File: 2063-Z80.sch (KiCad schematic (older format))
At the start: 76 parts, among them J1 Conn_01x05, J10 Conn_01x07, J2 DM3D-SF(41), J3 Conn_02x20_Counter_Clockwise, J4 Conn_02x05_Odd_Even, J5 Conn_02x05_Odd_Even, J6 0548190519, J7 Conn_02x13_Top_Bottom, J8 Conn_01x05, J9 Conn_01x02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

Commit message: BOM updates.
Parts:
- R1, R3, R5: Description (none) -> ‎CF18JT2K70‎; Digi-Key_PN (none) -> CF18JT2K70CT-ND
- R11, R12: Description (none) -> ‎CF18JT1K00‎; Digi-Key_PN (none) -> CF18JT1K00CT-ND‎
- R2, R4, R6: Description (none) -> ‎CF18JT4K70‎; Digi-Key_PN (none) -> CF18JT2K70CT-ND
- R8, R9: Description (none) -> ‎CF18JT680R‎; Digi-Key_PN (none) -> CF18JT680RCT-ND‎
- RN1, RN2, RN3, RN4, RN5: Description (none) -> ‎4609X-101-103LF‎
- U2: Description (none) -> ‎AS6C4008-55PIN‎; Digi-Key_PN (none) -> 1450-1178-5-ND‎
- U3: Description (none) -> ‎SST39SF010A-70-4C-PHE; Digi-Key_PN (none) -> SST39SF010A-70-4C-PHE-ND‎

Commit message: Add jumpers for getting the SIO baud rate clock direct from X2 (EZ-bypass the CTC) Missing white-slug on J10 Show R8 & R9 as 680 ohms on silkscreen Change part number of the NAND gate to 74HCT132E (Schmitt) Move reset button to the right (so can read silk labels on J10)
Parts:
- added J11: Conn_02x03_Odd_Even, Connector_PinHeader_2.54mm:PinHeader_2x03_P2.54mm_Vertical, symbol Connector_Generic:Conn_02x03_Odd_Even
- Q1: footprint Package_TO_SOT_THT:TO-92L_Inline -> Package_TO_SOT_THT:TO-92L
- U11: value 74LS00 -> 74HCT132E
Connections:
- net BAUD_CLK: now also J11.1 (Pin_1), J11.2 (Pin_2)
- net SIO_CLKA: now also J11.4 (Pin_4); no longer U4.8 (ZC/TO1)
- net SIO_CLKB: now also J11.3 (Pin_3); no longer U4.9 (ZC/TO2)
- new net CTC_CLKA: J11.6 (Pin_6), U4.8 (ZC/TO1)
- new net CTC_CLKB: J11.5 (Pin_5), U4.9 (ZC/TO2)
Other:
- note added: "BAUD Rate CLK Select"
- moved on the sheet: D1, D2, R8, R9, X1, X2

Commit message: Add another 74LS32 for 512K memory support. Move 3.3v reg on back under the SD card. Use surface-mount caps for 3.3v power. Add alternate SMT footprints for X1 and X2.
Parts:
- removed J9: Conn_01x02, Connector_PinHeader_2.54mm:PinHeader_1x02_P2.54mm_Vertical, symbol Connector_Generic:Conn_01x02
- removed R13: 10K, Resistor_THT:R_Axial_DIN0204_L3.6mm_D1.6mm_P5.08mm_Horizontal, symbol Device:R
- added U13: 74LS32, Package_DIP:DIP-14_W7.62mm_Socket, symbol 74xx:74LS32
- added Y1: XX, Oscillator:Oscillator_SMD_IQD_IQXO70-4Pin_7.5x5.0mm_HandSoldering, symbol dk_Oscillators:XLH536025_000000I
- added Y2: CSX-750FBC3686400T, Oscillator:Oscillator_SMD_IQD_IQXO70-4Pin_7.5x5.0mm_HandSoldering, symbol dk_Oscillators:XLH536025_000000I
- C17: footprint Capacitor_THT:C_Disc_D3.0mm_W2.0mm_P2.50mm -> Capacitor_SMD:C_0805_2012Metric_Pad1.18x1.45mm_HandSolder
- C18: footprint Capacitor_THT:CP_Radial_D5.0mm_P2.50mm -> Capacitor_SMD:C_0805_2012Metric_Pad1.18x1.45mm_HandSolder
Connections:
- net +5V: now also U13.14 (VCC), Y1.4 (VDD), Y2.4 (VDD)
- net A15: now also U13.1, U13.12, U13.4, U13.9; no longer U10.12, U10.9, U2.31 (A15)
- net BAUD_CLK: now also Y2.3 (OUT)
- net CLK: now also Y1.3 (OUT)
- net DISC_LED: now also U11.8; no longer U6.9 (O3)
- net GND: now also U10.12, U11.9, U13.7 (GND), Y1.2 (GND), Y2.2 (GND); no longer U2.1 (A18)
- net LO_BANK_A16: now also U6.15 (O5), U13.5; no longer U10.13, U6.16 (O6)
- net LO_BANK_A17: now also U6.16 (O6), U13.10; no longer U10.10, U6.19 (O7)
- net SD5_MOSI: now also U11.10
- net ~DTRA: now also U10.10, U10.9; no longer U11.10, U11.9
- net ~PRN_INIT: now also U10.8; no longer U11.8
- net ~PRN_LF: now also U10.11; no longer U6.15 (O5)
- net ~PRN_STROBE: now also U6.9 (O3); no longer U6.12 (O4)
- net ~RTSA: now reaches U5.17 (~RTSA)
- net ~RTSA: now also U10.13
- net A16 renamed BA16
- net BA16: now also U13.6; no longer U10.11
- net A17 renamed BA17
- net BA17: now also U13.8
- new net BA15: U13.3, U2.31 (A15)
- new net BA18: U13.11, U2.1 (A18)
- new net LO_BANK_A15: U13.2, U6.12 (O4)
- new net LO_BANK_A18: U13.13, U6.19 (O7)
- no-connect marks 33 -> 34
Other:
- note added: "3.6864MHZ"
- note added: "System Clock"
- note added: "Y1 is an alternate\n footprint for X1"
- note added: "Y2 is an alternate\n footprint for X2"
- note removed: "Remove J9 for 128K SRAM9"
- moved on the sheet: C10, C13, C14, C15, C16, C18, C19, C20, C21, C22, C23, C3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

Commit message: Fix inverted DISC_LED signal. Create composite oscillator footprints for X1 and X2. Tidy up the sensitive clock-tracks.
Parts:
- removed Y1: XX, Oscillator:Oscillator_SMD_IQD_IQXO70-4Pin_7.5x5.0mm_HandSoldering, symbol dk_Oscillators:XLH536025_000000I
- removed Y2: CSX-750FBC3686400T, Oscillator:Oscillator_SMD_IQD_IQXO70-4Pin_7.5x5.0mm_HandSoldering, symbol dk_Oscillators:XLH536025_000000I
- added C24: .1, Capacitor_SMD:C_0805_2012Metric_Pad1.15x1.40mm_HandSolder, symbol Device:C_Small
- X1: value ‎ECS-2100AX-049‎ -> ACH-10.000MHZ-EK; footprint Oscillator:Oscillator_DIP-8 -> jb-footprint:Oscillator_DIP-8_combo; Digi-Key_PN XC1159-ND‎ -> 535-9167-5-ND; MPN ECS-2100AX-049‎ -> ACH-10.000MHZ-EK
- X2: value ‎ECS-2100AX-049‎ -> ECS-2100A-018; footprint Oscillator:Oscillator_DIP-8 -> jb-footprint:Oscillator_DIP-8_combo; Digi-Key_PN XC1159-ND‎ -> XC231-ND‎; MPN ECS-2100AX-049‎ -> ‎ECS-2100A-018‎
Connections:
- net +5V: now also C24.1; no longer R8.2
- net DISC_LED: now also D2.2 (A); no longer D2.1 (K)
- net GND: now also R8.2, U10.10, C24.2; no longer U11.9
- net SD5_MOSI: no longer U11.10
- net ~DTRA: no longer U10.10
- net at R8.1: now also D2.1 (K); no longer D2.2 (A)
- net SD5_SSEL renamed ~SD5_SSEL
- net ~SD5_SSEL: now also U11.10, U11.9
- net SD_SSEL renamed ~SD_SSEL
- no-connect marks 34 -> 32
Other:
- note added: "1.8432MHZ"
- note added: "Shadow FLASH Select Logic"
- note removed: "3.6864MHZ"
- note removed: "4.9152MHZ"
- note removed: "FLASH Startup Select Logic"
- note removed: "Y1 is an alternate\n footprint for X1"
- note removed: "Y2 is an alternate\n footprint for X2"
- moved on the sheet: C20, C23, D2, D3, J11, J6, Q1, R11, R12, RN1, RN2, RN4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

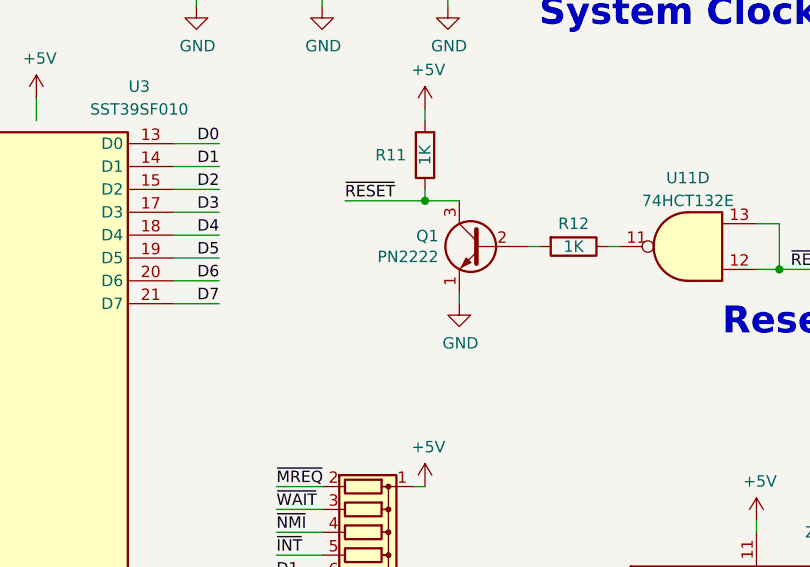
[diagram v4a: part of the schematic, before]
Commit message: Change .1uF parts on BOM.
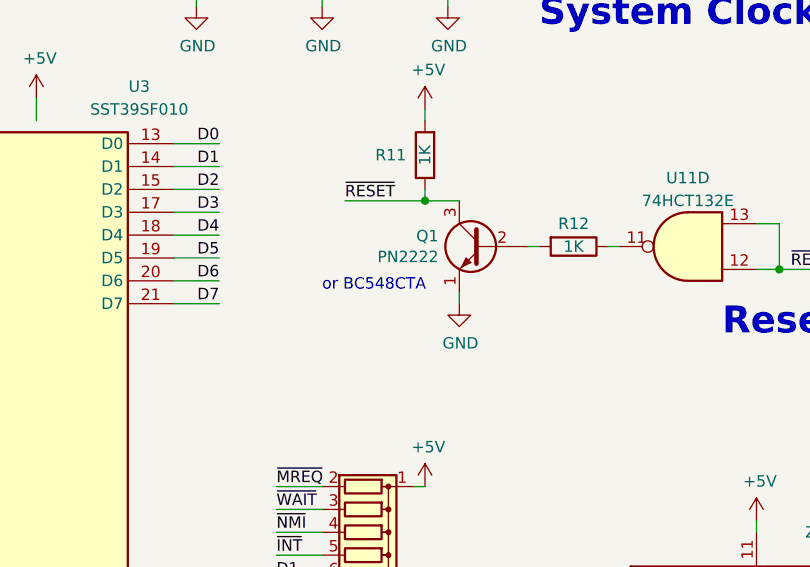
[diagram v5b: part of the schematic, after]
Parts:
- C1, C10, C11, C12, C13, C14, C15, C16, C2, C20, C21, C22, C23, C3, C4, C5, C6, C7, C8, C9: Digi-Key_PN 399-9976-ND -> 399-9859-1-ND‎; MPN (none) -> ‎C315C104M5U5TA7303‎
- C17: Digi-Key_PN 399-9976-ND -> (none)
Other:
- note added: "or ‎BC548CTA‎"
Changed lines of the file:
@@
 F 2 "Capacitor_THT:C_Disc_D3.0mm_W2.0mm_P2.50mm" H 4000 950 50  0001 C CNN
 F 3 "~" H 4000 950 50  0001 C CNN
-F 4 "399-9976-ND" H 4000 950 50  0001 C CNN "Digi-Key_PN"
+F 4 "399-9859-1-ND‎" H 4000 950 50  0001 C CNN "Digi-Key_PN"
+F 5 "‎C315C104M5U5TA7303‎" H 4000 950 50  0001 C CNN "MPN"
 	1    4000 950
 	1    0    0    -1
@@
 F 2 "Capacitor_THT:C_Disc_D3.0mm_W2.0mm_P2.50mm" H 4300 950 50  0001 C CNN
 F 3 "~" H 4300 950 50  0001 C CNN
-F 4 "399-9976-ND" H 4300 950 50  0001 C CNN "Digi-Key_PN"
+F 4 "399-9859-1-ND‎" H 4300 950 50  0001 C CNN "Digi-Key_PN"
+F 5 "‎C315C104M5U5TA7303‎" H 4300 950 50  0001 C CNN "MPN"
 	1    4300 950
 	1    0    0    -1
@@
 F 2 "Capacitor_THT:C_Disc_D3.0mm_W2.0mm_P2.50mm" H 4600 950 50  0001 C CNN
 F 3 "~" H 4600 950 50  0001 C CNN
-F 4 "399-9976-ND" H 4600 950 50  0001 C CNN "Digi-Key_PN"
+F 4 "399-9859-1-ND‎" H 4600 950 50  0001 C CNN "Digi-Key_PN"
+F 5 "‎C315C104M5U5TA7303‎" H 4600 950 50  0001 C CNN "MPN"
 	1    4600 950
 	1    0    0    -1
@@
 F 2 "Capacitor_THT:C_Disc_D3.0mm_W2.0mm_P2.50mm" H 4900 950 50  0001 C CNN
 F 3 "~" H 4900 950 50  0001 C CNN
-F 4 "399-9976-ND" H 4900 950 50  0001 C CNN "Digi-Key_PN"
+F 4 "399-9859-1-ND‎" H 4900 950 50  0001 C CNN "Digi-Key_PN"
+F 5 "‎C315C104M5U5TA7303‎" H 4900 950 50  0001 C CNN "MPN"
 	1    4900 950
 	1    0    0    -1
@@
 F 2 "Capacitor_THT:C_Disc_D3.0mm_W2.0mm_P2.50mm" H 5200 950 50  0001 C CNN
 F 3 "~" H 5200 950 50  0001 C CNN
-F 4 "399-9976-ND" H 5200 950 50  0001 C CNN "Digi-Key_PN"
+F 4 "399-9859-1-ND‎" H 5200 950 50  0001 C CNN "Digi-Key_PN"
+F 5 "‎C315C104M5U5TA7303‎" H 5200 950 50  0001 C CNN "MPN"
 	1    5200 950
 	1    0    0    -1
@@
 F 2 "Capacitor_THT:C_Disc_D3.0mm_W2.0mm_P2.50mm" H 7000 8400 50  0001 C CNN
 F 3 "~" H 7000 8400 50  0001 C CNN
-F 4 "399-9976-ND" H 7000 8400 50  0001 C CNN "Digi-Key_PN"
+F 4 "399-9859-1-ND‎" H 7000 8400 50  0001 C CNN "Digi-Key_PN"
+F 5 "‎C315C104M5U5TA7303‎" H 7000 8400 50  0001 C CNN "MPN"
 	1    7000 8400
 	1    0    0    -1
@@
 F 2 "Capacitor_THT:C_Disc_D3.0mm_W2.0mm_P2.50mm" H 9150 8350 50  0001 C CNN
 F 3 "~" H 9150 8350 50  0001 C CNN
-F 4 "399-9976-ND" H 9150 8350 50  0001 C CNN "Digi-Key_PN"
+F 4 "399-9859-1-ND‎" H 9150 8350 50  0001 C CNN "Digi-Key_PN"
+F 5 "‎C315C104M5U5TA7303‎" H 9150 8350 50  0001 C CNN "MPN"
 	1    9150 8350
 	1    0    0    -1
@@
 F 2 "Capacitor_THT:C_Disc_D3.0mm_W2.0mm_P2.50mm" H 9200 8750 50  0001 C CNN
 F 3 "~" H 9200 8750 50  0001 C CNN
-F 4 "399-9976-ND" H 9200 8750 50  0001 C CNN "Digi-Key_PN"
+F 4 "399-9859-1-ND‎" H 9200 8750 50  0001 C CNN "Digi-Key_PN"
+F 5 "‎C315C104M5U5TA7303‎" H 9200 8750 50  0001 C CNN "MPN"
 	1    9200 8750
 	0    1    1    0
@@
 F 2 "Capacitor_THT:C_Disc_D3.0mm_W2.0mm_P2.50mm" H 9200 9050 50  0001 C CNN
 F 3 "~" H 9200 9050 50  0001 C CNN
-F 4 "399-9976-ND" H 9200 9050 50  0001 C CNN "Digi-Key_PN"
+F 4 "399-9859-1-ND‎" H 9200 9050 50  0001 C CNN "Digi-Key_PN"
+F 5 "‎C315C104M5U5TA7303‎" H 9200 9050 50  0001 C CNN "MPN"
 	1    9200 9050
 	0    1    1    0
@@
 F 2 "Capacitor_THT:C_Disc_D3.0mm_W2.0mm_P2.50mm" H 5500 950 50  0001 C CNN
 F 3 "~" H 5500 950 50  0001 C CNN
-F 4 "399-9976-ND" H 5500 950 50  0001 C CNN "Digi-Key_PN"
+F 4 "399-9859-1-ND‎" H 5500 950 50  0001 C CNN "Digi-Key_PN"
+F 5 "‎C315C104M5U5TA7303‎" H 5500 950 50  0001 C CNN "MPN"
 	1    5500 950
 	-1   0    0    1
@@
 F 2 "Capacitor_THT:C_Disc_D3.0mm_W2.0mm_P2.50mm" H 5200 1550 50  0001 C CNN
 F 3 "~" H 5200 1550 50  0001 C CNN
-F 4 "399-9976-ND" H 5200 1550 50  0001 C CNN "Digi-Key_PN"
+F 4 "399-9859-1-ND‎" H 5200 1550 50  0001 C CNN "Digi-Key_PN"
+F 5 "‎C315C104M5U5TA7303‎" H 5200 1550 50  0001 C CNN "MPN"
 	1    5200 1550
 	1    0    0    -1
@@
 F 2 "Capacitor_THT:C_Disc_D3.0mm_W2.0mm_P2.50mm" H 5500 1550 50  0001 C CNN
 F 3 "~" H 5500 1550 50  0001 C CNN
-F 4 "399-9976-ND" H 5500 1550 50  0001 C CNN "Digi-Key_PN"
+F 4 "399-9859-1-ND‎" H 5500 1550 50  0001 C CNN "Digi-Key_PN"
+F 5 "‎C315C104M5U5TA7303‎" H 5500 1550 50  0001 C CNN "MPN"
 	1    5500 1550
 	1    0    0    -1
@@
 F 2 "Capacitor_THT:C_Disc_D3.0mm_W2.0mm_P2.50mm" H 3700 1550 50  0001 C CNN
 F 3 "~" H 3700 1550 50  0001 C CNN
-F 4 "399-9976-ND" H 3700 1550 50  0001 C CNN "Digi-Key_PN"
+F 4 "399-9859-1-ND‎" H 3700 1550 50  0001 C CNN "Digi-Key_PN"
+F 5 "‎C315C104M5U5TA7303‎" H 3700 1550 50  0001 C CNN "MPN"
 	1    3700 1550
 	1    0    0    -1
@@
 F 2 "Capacitor_THT:C_Disc_D3.0mm_W2.0mm_P2.50mm" H 4000 1550 50  0001 C CNN
 F 3 "~" H 4000 1550 50  0001 C CNN
-F 4 "399-9976-ND" H 4000 1550 50  0001 C CNN "Digi-Key_PN"
+F 4 "399-9859-1-ND‎" H 4000 1550 50  0001 C CNN "Digi-Key_PN"
+F 5 "‎C315C104M5U5TA7303‎" H 4000 1550 50  0001 C CNN "MPN"
 	1    4000 1550
 	1    0    0    -1
@@
 F 2 "Capacitor_THT:C_Disc_D3.0mm_W2.0mm_P2.50mm" H 4300 1550 50  0001 C CNN
 F 3 "~" H 4300 1550 50  0001 C CNN
-F 4 "399-9976-ND" H 4300 1550 50  0001 C CNN "Digi-Key_PN"
+F 4 "399-9859-1-ND‎" H 4300 1550 50  0001 C CNN "Digi-Key_PN"
+F 5 "‎C315C104M5U5TA7303‎" H 4300 1550 50  0001 C CNN "MPN"
 	1    4300 1550
 	1    0    0    -1
@@
 F 2 "Capacitor_THT:C_Disc_D3.0mm_W2.0mm_P2.50mm" H 4600 1550 50  0001 C CNN
 F 3 "~" H 4600 1550 50  0001 C CNN
-F 4 "399-9976-ND" H 4600 1550 50  0001 C CNN "Digi-Key_PN"
+F 4 "399-9859-1-ND‎" H 4600 1550 50  0001 C CNN "Digi-Key_PN"
+F 5 "‎C315C104M5U5TA7303‎" H 4600 1550 50  0001 C CNN "MPN"
 	1    4600 1550
 	1    0    0    -1
@@
 F 2 "Capacitor_SMD:C_0805_2012Metric_Pad1.18x1.45mm_HandSolder" H 13450 8200 50  0001 C CNN
 F 3 "~" H 13450 8200 50  0001 C CNN
-F 4 "399-9976-ND" H 13450 8200 50  0001 C CNN "Digi-Key_PN"
+F 4 "" H 13450 8200 50  0001 C CNN "Digi-Key_PN"
 	1    13450 8200
 	1    0    0    -1
@@
 F 2 "Capacitor_THT:C_Disc_D3.0mm_W2.0mm_P2.50mm" H 4900 1550 50  0001 C CNN
 F 3 "~" H 4900 1550 50  0001 C CNN
-F 4 "399-9976-ND" H 4900 1550 50  0001 C CNN "Digi-Key_PN"
+F 4 "399-9859-1-ND‎" H 4900 1550 50  0001 C CNN "Digi-Key_PN"
+F 5 "‎C315C104M5U5TA7303‎" H 4900 1550 50  0001 C CNN "MPN"
 	1    4900 1550
 	1    0    0    -1
@@
 F 2 "Capacitor_THT:C_Disc_D3.0mm_W2.0mm_P2.50mm" H 10100 3050 50  0001 C CNN
 F 3 "~" H 10100 3050 50  0001 C CNN
-F 4 "399-9976-ND" H 10100 3050 50  0001 C CNN "Digi-Key_PN"
+F 4 "399-9859-1-ND‎" H 10100 3050 50  0001 C CNN "Digi-Key_PN"
+F 5 "‎C315C104M5U5TA7303‎" H 10100 3050 50  0001 C CNN "MPN"
 	1    10100 3050
 	1    0    0    -1
@@
 F 2 "Capacitor_THT:C_Disc_D3.0mm_W2.0mm_P2.50mm" H 3700 950 50  0001 C CNN
 F 3 "~" H 3700 950 50  0001 C CNN
-F 4 "399-9976-ND" H 3700 950 50  0001 C CNN "Digi-Key_PN"
+F 4 "399-9859-1-ND‎" H 3700 950 50  0001 C CNN "Digi-Key_PN"
+F 5 "‎C315C104M5U5TA7303‎" H 3700 950 50  0001 C CNN "MPN"
 	1    3700 950
 	1    0    0    -1
@@
 F 2 "Capacitor_THT:C_Disc_D3.0mm_W2.0mm_P2.50mm" H 5850 950 50  0001 C CNN
 F 3 "~" H 5850 950 50  0001 C CNN
-F 4 "399-9976-ND" H 5850 950 50  0001 C CNN "Digi-Key_PN"
+F 4 "399-9859-1-ND‎" H 5850 950 50  0001 C CNN "Digi-Key_PN"
+F 5 "‎C315C104M5U5TA7303‎" H 5850 950 50  0001 C CNN "MPN"
 	1    5850 950
 	1    0    0    -1
@@
 	1    0    0    -1
 $EndComp
+Text Notes 7250 3050 0    50   ~ 0
+or ‎BC548CTA‎
 $EndSCHEMATC

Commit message: Add pull up to SIO (and CTC) IEI.
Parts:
- added R10, R13: 10K, Resistor_THT:R_Axial_DIN0204_L3.6mm_D1.6mm_P5.08mm_Horizontal, symbol Device:R
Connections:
- net +5V: now also R10.2, R13.2; no longer U4.13 (IEI)
- net CTC_IEO: now also R10.1
- new net: R13.1, U4.13 (IEI)
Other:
- note added: "Populate R10 when the CTC is not present. \nElse optional."
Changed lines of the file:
@@
 	11550 6350 11900 6350
-Wire Wire Line
-	11550 6250 11900 6250
 Wire Wire Line
 	11550 6150 11900 6150
@@
 Text Label 7700 6400 2    50   ~ 0
 A0
-$Comp
-L power:+5V #PWR0143
-U 1 1 62D73A3F
-P 5900 7050
-F 0 "#PWR0143" H 5900 6900 50  0001 C CNN
-F 1 "+5V" H 5915 7223 50  0000 C CNN
-F 2 "" H 5900 7050 50  0001 C CNN
-F 3 "" H 5900 7050 50  0001 C CNN
-	1    5900 7050
-	1    0    0    -1
-$EndComp
-Wire Wire Line
-	6350 7050 5900 7050
 Text Label 6000 7150 0    50   ~ 0
 CTC_IEO
@@
 Text Notes 7250 3050 0    50   ~ 0
 or ‎BC548CTA‎
+$Comp
+L Device:R R10
+U 1 1 614B473D
+P 11350 6100
+F 0 "R10" V 11450 6100 50  0000 C CNN
+F 1 "10K" V 11350 6100 50  0000 C CNN
+F 2 "Resistor_THT:R_Axial_DIN0204_L3.6mm_D1.6mm_P5.08mm_Horizontal" V 11280 6100 50  0001 C CNN
+F 3 "~" H 11350 6100 50  0001 C CNN
+	1    11350 6100
+	-1   0    0    1
+$EndComp
+Wire Wire Line
+	11350 6250 11900 6250
+Wire Wire Line
+	11350 5950 11350 5900
+$Comp
+L power:+5V #PWR014
+U 1 1 615C4A3C
+P 11350 5900
+F 0 "#PWR014" H 11350 5750 50  0001 C CNN
+F 1 "+5V" H 11365 6073 50  0000 C CNN
+F 2 "" H 11350 5900 50  0001 C CNN
+F 3 "" H 11350 5900 50  0001 C CNN
+	1    11350 5900
+	1    0    0    -1
+$EndComp
+$Comp
+L Device:R R13
+U 1 1 615CB44E
+P 5800 6900
+F 0 "R13" V 5700 6900 50  0000 C CNN
+F 1 "10K" V 5800 6900 50  0000 C CNN
+F 2 "Resistor_THT:R_Axial_DIN0204_L3.6mm_D1.6mm_P5.08mm_Horizontal" V 5730 6900 50  0001 C CNN
+F 3 "~" H 5800 6900 50  0001 C CNN
+	1    5800 6900
+	-1   0    0    1
+$EndComp
+Wire Wire Line
+	5800 6750 5800 6700
+$Comp
+L power:+5V #PWR015
+U 1 1 615CB455
+P 5800 6700
+F 0 "#PWR015" H 5800 6550 50  0001 C CNN
+F 1 "+5V" H 5815 6873 50  0000 C CNN
+F 2 "" H 5800 6700 50  0001 C CNN
+F 3 "" H 5800 6700 50  0001 C CNN
+	1    5800 6700
+	1    0    0    -1
+$EndComp
+Wire Wire Line
+	5800 7050 6350 7050
+Text Notes 11400 5650 1    39   ~ 0
+Populate R10 when the CTC is not present. \nElse optional.
 $EndSCHEMATC

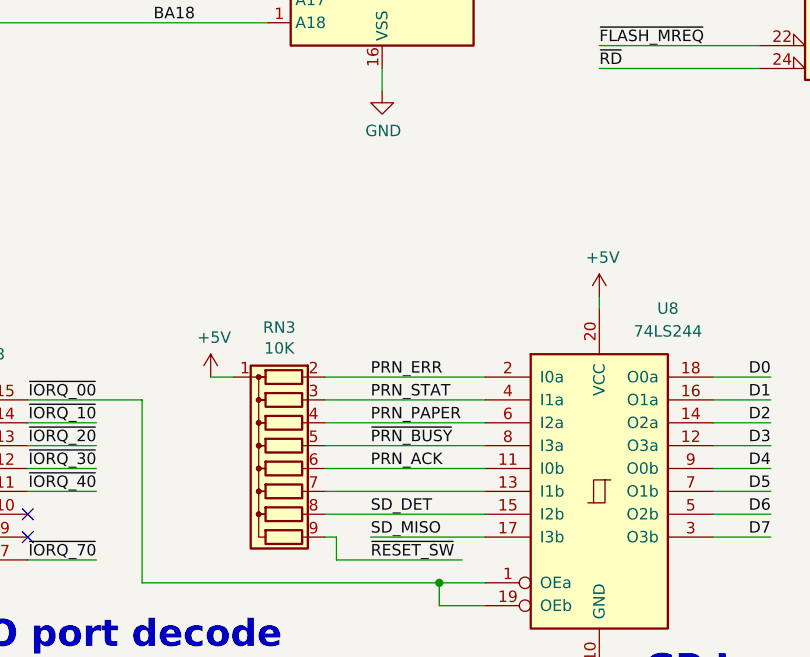
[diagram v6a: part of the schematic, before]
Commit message: Ass USER1 jumper on an otherwise unused input.
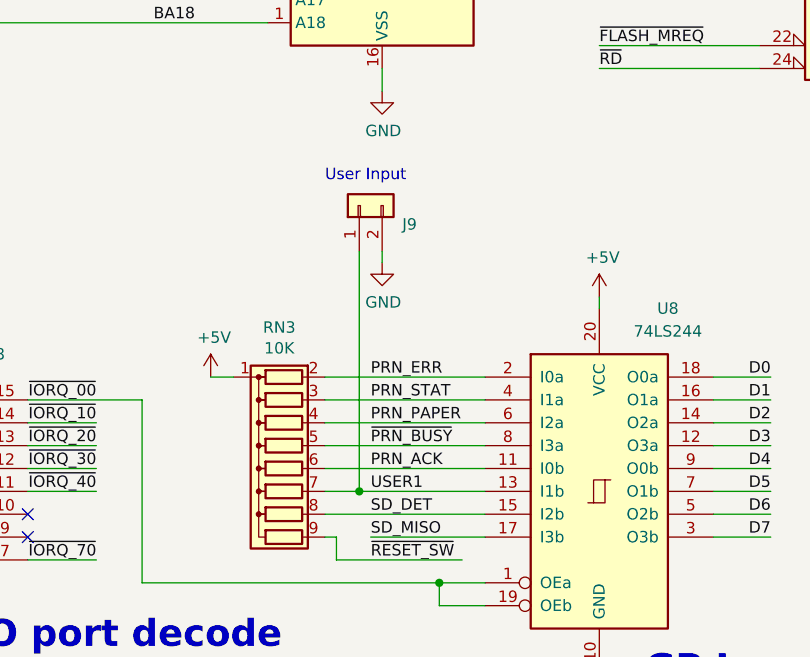
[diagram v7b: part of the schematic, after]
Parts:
- added J9: Conn_01x02, Connector_PinHeader_2.54mm:PinHeader_1x02_P2.54mm_Vertical, symbol Connector_Generic:Conn_01x02
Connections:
- net GND: now also J9.2 (Pin_2)
- net USER1: now reaches RN3.7 (R6), U8.13 (I1b)
- net USER1: now also J9.1 (Pin_1)
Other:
- note added: "User Input"
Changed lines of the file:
@@
 	3500 6650 4200 6650
 Wire Wire Line
-	3500 6550 4200 6550
+	3500 6550 3650 6550
 Wire Wire Line
 	3500 6450 4200 6450
@@
 Text Notes 11400 5650 1    39   ~ 0
 Populate R10 when the CTC is not present. \nElse optional.
+Text Label 3700 6550 0    50   ~ 0
+USER1
+Wire Wire Line
+	3650 6550 3650 5500
+Connection ~ 3650 6550
+Wire Wire Line
+	3650 6550 4200 6550
+$Comp
+L Connector_Generic:Conn_01x02 J9
+U 1 1 6157539A
+P 3650 5300
+F 0 "J9" V 3568 5112 50  0000 R CNN
+F 1 "Conn_01x02" V 3523 5112 50  0001 R CNN
+F 2 "Connector_PinHeader_2.54mm:PinHeader_1x02_P2.54mm_Vertical" H 3650 5300 50  0001 C CNN
+F 3 "~" H 3650 5300 50  0001 C CNN
+	1    3650 5300
+	0    -1   -1   0
+$EndComp
+$Comp
+L power:GND #PWR018
+U 1 1 61603B1F
+P 3750 5550
+F 0 "#PWR018" H 3750 5300 50  0001 C CNN
+F 1 "GND" H 3755 5377 50  0000 C CNN
+F 2 "" H 3750 5550 50  0001 C CNN
+F 3 "" H 3750 5550 50  0001 C CNN
+	1    3750 5550
+	1    0    0    -1
+$EndComp
+Wire Wire Line
+	3750 5550 3750 5500
+Text Notes 3500 5200 0    50   ~ 0
+User Input
 $EndSCHEMATC
